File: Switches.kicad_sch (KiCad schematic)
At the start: 26 parts, among them J3 INDICATOR_SWITCH_OUT

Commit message: fixed
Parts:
- removed GR_SW1: GEAR_SW_12V, switched:3posSlideToggle, symbol Switch:SW_SPDT_MSM
- added GEAR_SW_12V1: GR_SW1, switched:3posSlideToggle, symbol Switch:SW_SP3T
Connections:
- net +12V: now also GEAR_SW_12V1.1, GEAR_SW_12V1.4
- net FWD_SW: now also GEAR_SW_12V1.2
- net REV_SW: now also GEAR_SW_12V1.3
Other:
- note removed: "Nuetral"

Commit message: Johnathan
Added FET for horn, fixed other stuff, etc
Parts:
- C1, C2, C3, C4, C5, C6, C7, C8, C9: footprint Capacitor_SMD:C_0805_2012Metric -> Capacitor_SMD:C_0805_2012Metric_Pad1.18x1.45mm_HandSolder
- R1, R2, R3, R4, R5, R6, R7, R8, R9: footprint Resistor_SMD:R_0805_2012Metric -> Resistor_SMD:R_0805_2012Metric_Pad1.20x1.40mm_HandSolder
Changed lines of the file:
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@@
 			)
 		)
-		(property "Footprint" "Capacitor_SMD:C_0805_2012Metric"
+		(property "Footprint" "Capacitor_SMD:C_0805_2012Metric_Pad1.18x1.45mm_HandSolder"
 			(at 228.6 43.18 0)
 			(effects
@@
 			)
 		)
-		(property "Footprint" "Capacitor_SMD:C_0805_2012Metric"
+		(property "Footprint" "Capacitor_SMD:C_0805_2012Metric_Pad1.18x1.45mm_HandSolder"
 			(at 105.41 57.15 0)
 			(effects
@@
 			)
 		)
-		(property "Footprint" "Resistor_SMD:R_0805_2012Metric"
+		(property "Footprint" "Resistor_SMD:R_0805_2012Metric_Pad1.20x1.40mm_HandSolder"
 			(at 178.816 61.214 90)
 			(effects
@@
 			)
 		)
-		(property "Footprint" "Resistor_SMD:R_0805_2012Metric"
+		(property "Footprint" "Resistor_SMD:R_0805_2012Metric_Pad1.20x1.40mm_HandSolder"
 			(at 45.466 122.174 90)
 			(effects
@@
 			)
 		)
-		(property "Footprint" "Capacitor_SMD:C_0805_2012Metric"
+		(property "Footprint" "Capacitor_SMD:C_0805_2012Metric_Pad1.18x1.45mm_HandSolder"
 			(at 40.64 121.92 0)
 			(effects
@@
 			)
 		)
-		(property "Footprint" "Capacitor_SMD:C_0805_2012Metric"
+		(property "Footprint" "Capacitor_SMD:C_0805_2012Metric_Pad1.18x1.45mm_HandSolder"
 			(at 185.42 60.96 0)
 			(effects
@@
 			)
 		)
-		(property "Footprint" "Resistor_SMD:R_0805_2012Metric"
+		(property "Footprint" "Resistor_SMD:R_0805_2012Metric_Pad1.20x1.40mm_HandSolder"
 			(at 49.276 63.754 90)
 			(effects
@@
 			)
 		)
-		(property "Footprint" "Capacitor_SMD:C_0805_2012Metric"
+		(property "Footprint" "Capacitor_SMD:C_0805_2012Metric_Pad1.18x1.45mm_HandSolder"
 			(at 77.47 121.92 0)
 			(effects
@@
 			)
 		)
-		(property "Footprint" "Resistor_SMD:R_0805_2012Metric"
+		(property "Footprint" "Resistor_SMD:R_0805_2012Metric_Pad1.20x1.40mm_HandSolder"
 			(at 186.944 40.386 90)
 			(effects
@@
 			)
 		)
-		(property "Footprint" "Resistor_SMD:R_0805_2012Metric"
+		(property "Footprint" "Resistor_SMD:R_0805_2012Metric_Pad1.20x1.40mm_HandSolder"
 			(at 230.124 60.706 90)
 			(effects
@@
 			)
 		)
-		(property "Footprint" "Resistor_SMD:R_0805_2012Metric"
+		(property "Footprint" "Resistor_SMD:R_0805_2012Metric_Pad1.20x1.40mm_HandSolder"
 			(at 80.264 121.666 90)
 			(effects
@@
 			)
 		)
-		(property "Footprint" "Resistor_SMD:R_0805_2012Metric"
+		(property "Footprint" "Resistor_SMD:R_0805_2012Metric_Pad1.20x1.40mm_HandSolder"
 			(at 67.564 63.246 90)
 			(effects
@@
 			)
 		)
-		(property "Footprint" "Capacitor_SMD:C_0805_2012Metric"
+		(property "Footprint" "Capacitor_SMD:C_0805_2012Metric_Pad1.18x1.45mm_HandSolder"
 			(at 227.33 60.96 0)
 			(effects
@@
 			)
 		)
-		(property "Footprint" "Resistor_SMD:R_0805_2012Metric"
+		(property "Footprint" "Resistor_SMD:R_0805_2012Metric_Pad1.20x1.40mm_HandSolder"
 			(at 108.204 56.896 90)
 			(effects
@@
 			)
 		)
-		(property "Footprint" "Resistor_SMD:R_0805_2012Metric"
+		(property "Footprint" "Resistor_SMD:R_0805_2012Metric_Pad1.20x1.40mm_HandSolder"
 			(at 231.394 42.926 90)
 			(effects
@@
 			)
 		)
-		(property "Footprint" "Capacitor_SMD:C_0805_2012Metric"
+		(property "Footprint" "Capacitor_SMD:C_0805_2012Metric_Pad1.18x1.45mm_HandSolder"
 			(at 64.77 63.5 0)
 			(effects
@@
 			)
 		)
-		(property "Footprint" "Capacitor_SMD:C_0805_2012Metric"
+		(property "Footprint" "Capacitor_SMD:C_0805_2012Metric_Pad1.18x1.45mm_HandSolder"
 			(at 181.61 40.64 0)
 			(effects
@@
 			)
 		)
-		(property "Footprint" "Capacitor_SMD:C_0805_2012Metric"
+		(property "Footprint" "Capacitor_SMD:C_0805_2012Metric_Pad1.18x1.45mm_HandSolder"
 			(at 52.07 63.5 0)
 			(effects

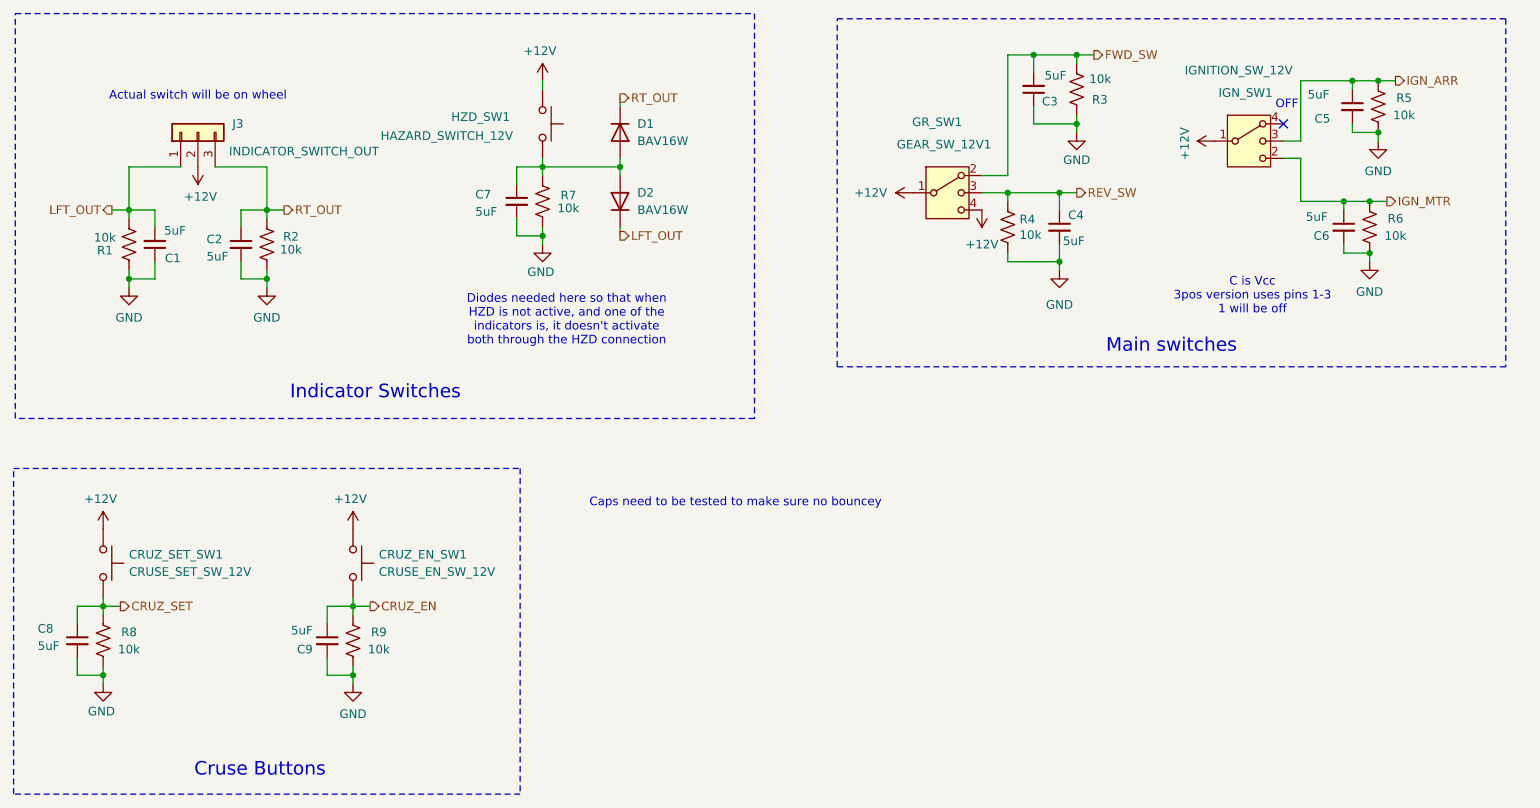
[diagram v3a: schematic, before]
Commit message: make ign off cruz en or some shit
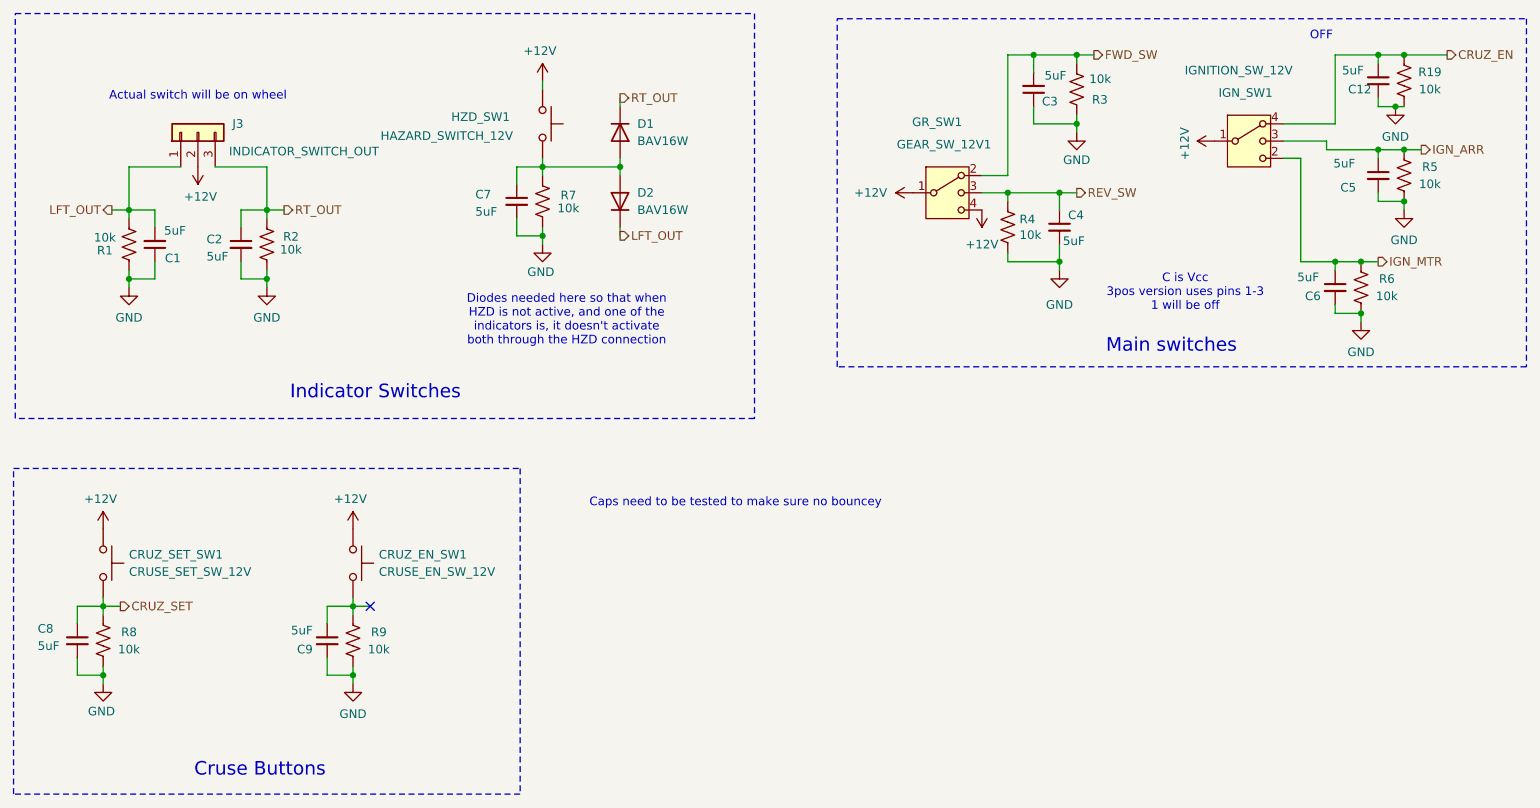
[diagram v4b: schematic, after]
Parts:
- added C12: 5uF, Capacitor_SMD:C_0805_2012Metric_Pad1.18x1.45mm_HandSolder, symbol Device:C_Small
- added R19: 10k, Resistor_SMD:R_0805_2012Metric_Pad1.20x1.40mm_HandSolder, symbol Device:R_US
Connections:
- net CRUZ_EN: now also IGN_SW1.4, C12.1, R19.2; no longer C9.1, CRUZ_EN_SW1.2, R9.2
- net GND: now also C12.2, R19.1
- new net: C9.1, CRUZ_EN_SW1.2, R9.2
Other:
- moved on the sheet: C5, C6, R5, R6
